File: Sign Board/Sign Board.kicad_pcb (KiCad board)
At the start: 2 copper layers, 32 x 68.5 mm, 18 parts, among them J1 Conn_01x03_Socket, J2 Conn_01x03_Pin, J3 Conn_01x03_Pin, J4 Conn_01x03_Pin, J5 Conn_01x03_Pin, J6 Conn_01x03_Pin

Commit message: Break Everything
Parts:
- removed F6: Fuse, Fuse:Fuseholder_Blade_Mini_Keystone_3568
- moved 2024 68.7 mm to (208.6, 123.5)
- moved J1 46.1 mm to (206.7, 66.5)
- moved F1 33.4 mm to (217.5, 70.0)
- moved F2 33.4 mm to (217.5, 83.9)
- moved F3 33.4 mm to (217.5, 97.8)
- moved F4 33.4 mm to (217.5, 111.7)
- moved F5 33.4 mm to (217.5, 125.6)
- moved JP1 28.5 mm to (217.5, 62.5)
- moved JP2 28.5 mm to (217.5, 76.4)
- moved JP3 28.5 mm to (217.5, 90.3)
- moved JP4 28.5 mm to (217.5, 104.2)
- moved JP5 28.5 mm to (217.5, 118.1)
- moved J2 23.7 mm to (222.5, 57.5)
- moved J3 23.7 mm to (222.5, 71.4)
- moved J4 23.7 mm to (222.5, 85.3)
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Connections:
- F1 pad 1: Net-(F1-Pad1) -> Net-(J1-Pin_3)
- F2 pad 1: Net-(F1-Pad1) -> Net-(J1-Pin_3)
- F3 pad 1: Net-(F1-Pad1) -> Net-(J1-Pin_3)
- F4 pad 1: Net-(F1-Pad1) -> Net-(J1-Pin_3)
- F5 pad 1: Net-(F1-Pad1) -> Net-(J1-Pin_3)
- J2 pad 3: Net-(J1-Pin_3) -> Net-(J1-Pin_1)
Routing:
- net Net-(J1-Pin_2): track 92.0 -> 0.00 mm, vias 5 -> 20
- net Net-(F1-Pad1): track 76.6 -> 0.00 mm
- net Net-(J1-Pin_3): track 72.0 -> 17.5 mm
- net Net-(J2-Pin_1): track 13.8 -> 3.76 mm
- net Net-(J6-Pin_1): track 13.8 -> 3.76 mm
- net Net-(J5-Pin_1): track 13.8 -> 3.76 mm
- net Net-(J4-Pin_1): track 13.8 -> 3.76 mm
- net Net-(J3-Pin_1): track 13.8 -> 3.76 mm
- net Net-(J5-Pin_3): track 22.5 -> 15.7 mm
- net Net-(J3-Pin_3): track 22.2 -> 15.7 mm
- net Net-(J6-Pin_2): track 9.35 -> 4.35 mm
- net Net-(J5-Pin_2): track 9.35 -> 4.35 mm
- net Net-(J4-Pin_2): track 8.35 -> 4.35 mm
- net Net-(J3-Pin_2): track 8.35 -> 4.35 mm
- net Net-(J2-Pin_2): track 8.35 -> 4.35 mm
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- added copper zone on F.Cu, net Net-(J1-Pin_3)
- removed copper zone on F.Cu, net Net-(F1-Pad1)
- removed copper zone on F.Cu, net Net-(J1-Pin_1)
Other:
- board size 32 x 68.5 mm -> 22.5 x 68.7 mm
- board text added: "DATA GND +5v"

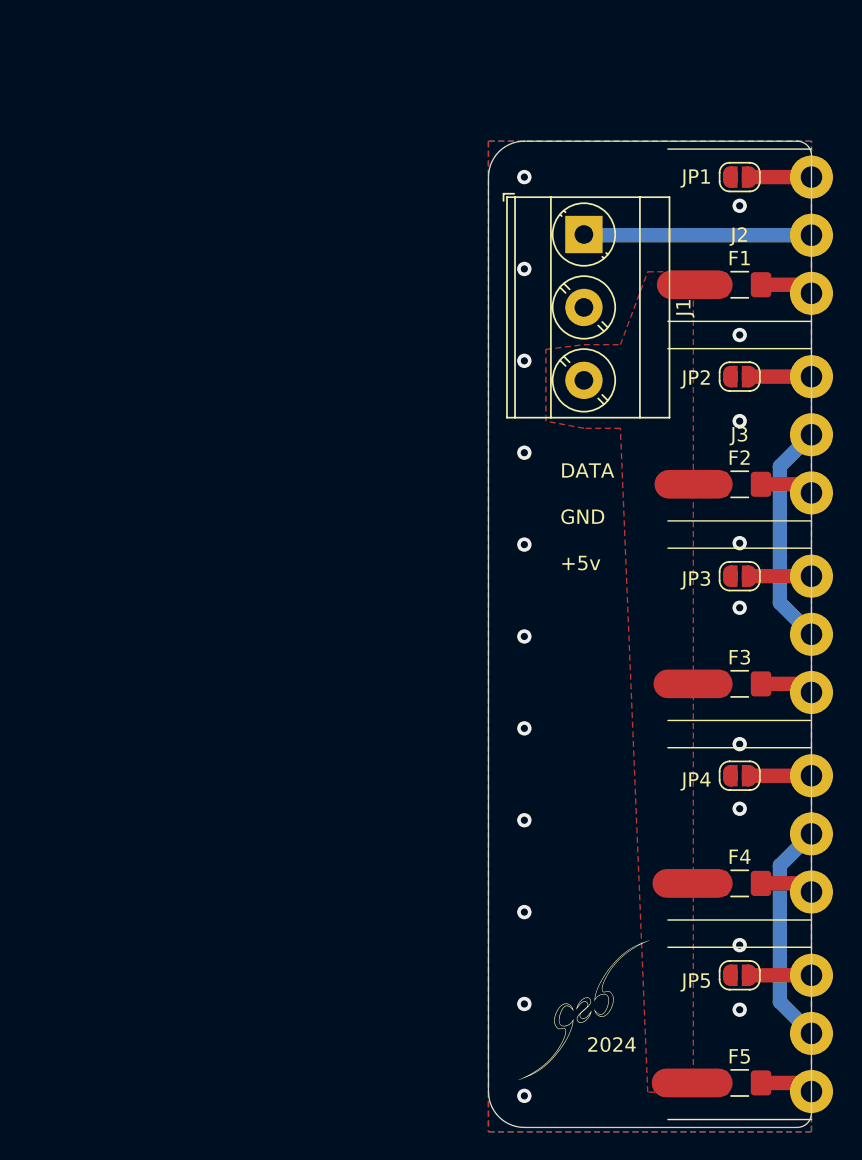
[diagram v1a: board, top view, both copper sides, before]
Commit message: Reworked GND/Power planes and adjusted schematic to match application
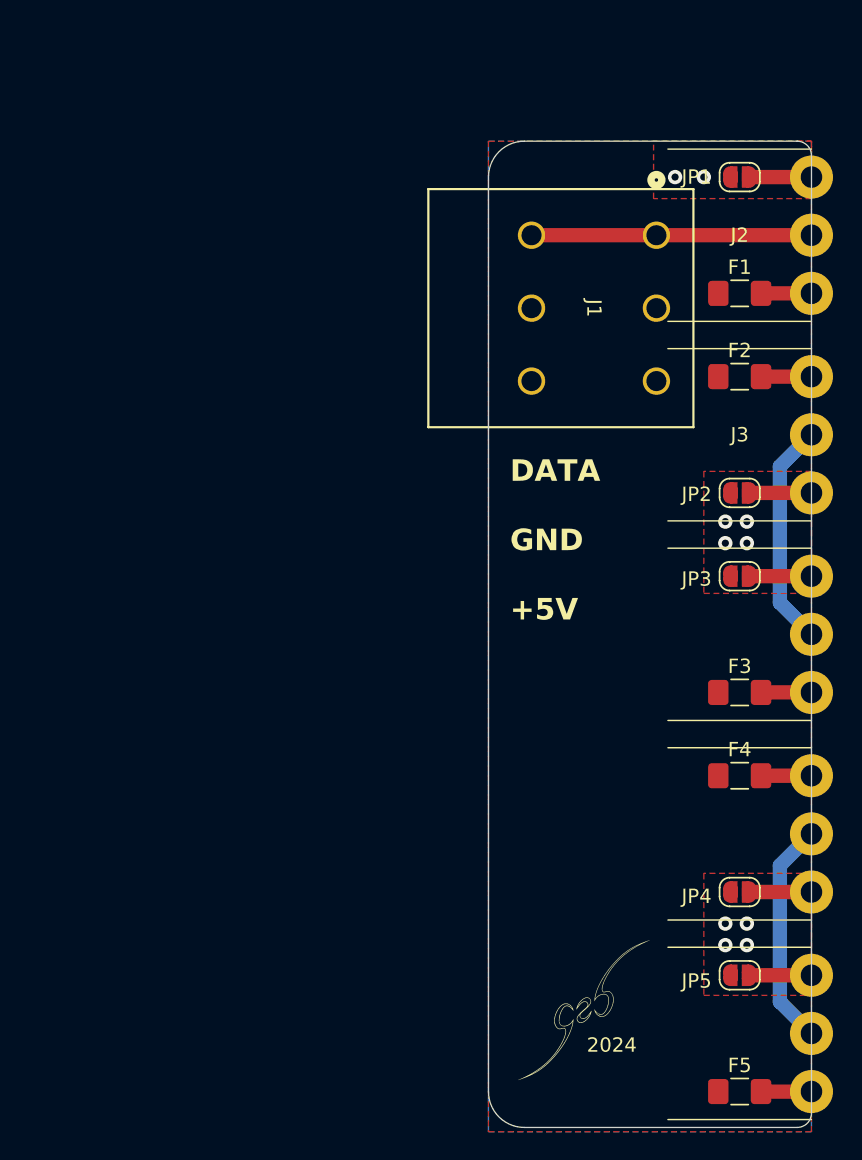
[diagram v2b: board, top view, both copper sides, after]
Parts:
- J1: footprint TerminalBlock_Phoenix:TerminalBlock_Phoenix_MKDS-3-3-5.08_1x03_P5.08mm_Horizontal -> footprints:CONN_1017492
- moved J1 10.8 mm to (203.0, 76.7)
- moved JP2 8.10 mm to (217.5, 84.5)
- moved JP4 8.10 mm to (217.5, 112.3)
- moved F2 7.50 mm to (217.5, 76.4)
- moved F4 7.50 mm to (217.5, 104.2)
- moved F3 0.60 mm to (217.5, 98.4)
- moved F5 0.60 mm to (217.5, 126.2)
- moved F1 0.60 mm to (217.5, 70.6)
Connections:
- F1 pad 1: Net-(J1-Pin_3) -> Net-(F1-Pad1)
- F2 pad 1: Net-(J1-Pin_3) -> Net-(F1-Pad1)
- F2 pad 2: Net-(J3-Pin_1) -> Net-(J3-Pin_2)
- F3 pad 1: Net-(J1-Pin_3) -> Net-(F1-Pad1)
- F4 pad 1: Net-(J1-Pin_3) -> Net-(F1-Pad1)
- F4 pad 2: Net-(J5-Pin_1) -> Net-(J5-Pin_2)
- F5 pad 1: Net-(J1-Pin_3) -> Net-(F1-Pad1)
- J1 pad 1: Net-(J1-Pin_1) -> Net-(J2-Pin_3)
- J1 pad 2: Net-(J1-Pin_2) -> Net-(J2-Pin_3)
- J1 pad 3: Net-(J1-Pin_3) -> Net-(JP1-A)
- J2 pad 3: Net-(J1-Pin_1) -> Net-(J2-Pin_3)
- JP1 pad 1: Net-(J1-Pin_2) -> Net-(JP1-A)
- JP2 pad 1: Net-(J1-Pin_2) -> Net-(JP1-A)
- JP2 pad 2: Net-(J3-Pin_2) -> Net-(J3-Pin_1)
- JP3 pad 1: Net-(J1-Pin_2) -> Net-(JP1-A)
- JP4 pad 1: Net-(J1-Pin_2) -> Net-(JP1-A)
- JP4 pad 2: Net-(J5-Pin_2) -> Net-(J5-Pin_1)
- JP5 pad 1: Net-(J1-Pin_2) -> Net-(JP1-A)
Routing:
- net Net-(J2-Pin_3): track 0.00 -> 18.5 mm
- net Net-(J1-Pin_3): track 17.5 -> 0.00 mm
- net Net-(J1-Pin_1): track 15.9 -> 0.00 mm
- net Net-(J5-Pin_2): track 4.35 -> 2.51 mm
- net Net-(J3-Pin_2): track 4.35 -> 2.51 mm
- net Net-(J6-Pin_1): track 3.76 -> 2.51 mm
- net Net-(J4-Pin_1): track 3.76 -> 2.51 mm
- net Net-(J2-Pin_1): track 3.76 -> 2.51 mm
- net Net-(JP1-A): vias 0 -> 10
- net Net-(J1-Pin_2): vias 20 -> 0
- added copper zone on F.Cu, net Net-(F1-Pad1)
- added copper zone on B.Cu, net Net-(JP1-A)
- added copper zone on F.Cu, net Net-(JP1-A)
- removed copper zone on B.Cu, net Net-(J1-Pin_2)
- removed copper zone on F.Cu, net Net-(J1-Pin_2)
- removed copper zone on F.Cu, net Net-(J1-Pin_3)
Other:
- board text added: "DATA GND +5V"
- board text removed: "DATA GND +5v"
